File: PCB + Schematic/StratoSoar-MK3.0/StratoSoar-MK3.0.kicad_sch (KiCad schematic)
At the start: 108 parts, among them J1 Power, J10 SWD, J11 Signal, J12 Rudder, J15 Parachute, J16 Elevator, J18 USB-C, J2 Battery, J3 USB-C, J4 J Link, J8 Button, Q1 DMN1019USN-13, Q2 2N3906, Q3 DMN1019USN-13, Q4 DMN1019USN-13, Q5 2N3906, Q6 2N3906, SW1 RESET, SW2 PWR_SW, SW4 RESET, SW5 EEPROM, U11 DSK321STD, U2 ATSAMD21G18A-A, U3 MCP1700x-330xxTT, U4 ATSAMD21G18A-A, U5 BME280, U6 AT24C512C-SSHD-T, U7 ATXK-H11-E-32.768, U8 MAX-M10S, U9 MPU-9250, Y2 32.768kHz

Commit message: Commit
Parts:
- removed J10: SWD, Connector_PinHeader_2.54mm:PinHeader_1x05_P2.54mm_Vertical, symbol Connector_Generic:Conn_01x05
- added C1: 10 uF, symbol Device:C_Small
- added C2: 100 nF, symbol Device:C_Small
- added J5: Antenna, symbol Connector_Generic:Conn_01x01
- added U1: Ra-01, RF_Module:Ai-Thinker-Ra-01-LoRa, symbol RF_Module:Ai-Thinker-Ra-01
- AE1: value 1575AT43A0040001E -> 1575AT43A0040E
- C30, C32, C33: value 47uF -> 47 uF
- R11, R12, R17, R18, R20, R21: value 10K -> 10 K
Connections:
- net +3.3V: now also C1.1, C2.1, U1.3 (VDD)
- net A3: no longer J11.1 (Pin_1), J8.1 (Pin_1)
- net A4: no longer J11.2 (Pin_2)
- net A5: no longer J11.3 (Pin_3)
- net CS: now also U1.15 (~{NSS})
- net GND: now also C1.2, C2.2, U1.16 (GND), U1.2 (GND), U1.9 (GND)
- net MISO: now also U1.13 (MISO)
- net MOSI: now also U1.14 (MOSI)
- net SCK: now also U1.12 (SCK)
- net USB_IN: now also C4.1, J3.A4 (VBUS), J3.A9 (VBUS), J3.B4 (VBUS), J3.B9 (VBUS)
- net VCC: now also C30.1, C32.1, C33.1, J12.2 (Pin_2), J15.2 (Pin_2), J16.2 (Pin_2)
- removed net +5V: C30.1, C32.1, C33.1, C4.1, J12.2 (Pin_2), J15.2 (Pin_2), J16.2 (Pin_2), J3.A4 (VBUS), J3.A9 (VBUS), J3.B4 (VBUS), J3.B9 (VBUS)
- net AT_SCL: no longer names the net of J11.9 (Pin_9)
- net AT_SDA: no longer names the net of J11.8 (Pin_8)
- new net: J5.1 (Pin_1), U1.1 (ANT)
- new net LORA_RST: U1.4 (~{RESET})
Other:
- note added: "- Add ATGM336"
- note added: "LoRa module"
- note added: "RF"
- moved on the sheet: AE1, C20, C21, C22, C23, C24, C30, C33, D6, H1, H2, H3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

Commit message: IMU stuff
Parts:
- removed C32: 47 uF, Capacitor_Tantalum_SMD:CP_EIA-3528-21_Kemet-B, symbol Device:C_Polarized_Small
- removed C35: 10nF, Capacitor_SMD:C_0805_2012Metric_Pad1.18x1.45mm_HandSolder, symbol Device:C_Small
- removed C36, C42: 100nF, Capacitor_SMD:C_0805_2012Metric_Pad1.18x1.45mm_HandSolder, symbol Device:C_Small
- removed J15: Parachute, Connector_PinHeader_2.54mm:PinHeader_1x03_P2.54mm_Vertical, symbol Connector_Generic:Conn_01x03
- removed Q3: DMN1019USN-13, Package_TO_SOT_SMD:SC-59_Handsoldering, symbol Transistor_FET:DMN1019USN-13
- removed Q5: 2N3906, Package_TO_SOT_SMD:SOT-23-3, symbol Transistor_BJT:2N3906
- removed R17, R20: 10 K, Resistor_SMD:R_0805_2012Metric_Pad1.20x1.40mm_HandSolder, symbol Device:R
- removed R22: 10, Resistor_SMD:R_0805_2012Metric_Pad1.20x1.40mm_HandSolder, symbol Device:R
- removed U9: MPU-9250, Sensor_Motion:InvenSense_QFN-24_3x3mm_P0.4mm, symbol Sensor_Motion:MPU-9250
- added C10, C3, C9: 100 nF, Capacitor_SMD:C_0402_1005Metric, symbol symbols:C_Small
- added C12, C13: 1 uF, Capacitor_SMD:C_0402_1005Metric, symbol symbols:C_Small
- added Q7, Q8, Q9: BSS138, Package_TO_SOT_SMD:SOT-23, symbol symbols:BSS138
- added R13, R19, R29, R30, R31, R32: 10 K, Resistor_SMD:R_0402_1005Metric, symbol symbols:R_Small
- added U10: ICM-20948, Sensor_Motion:InvenSense_QFN-24_3x3mm_P0.4mm, symbol symbols:MPU-9250
- added U9: CJ6206B18M, Package_TO_SOT_SMD:SOT-23-5, symbol symbols:CJ6206B18M
- Q2: value 2N3906 -> MMBT3906
- R11: footprint Resistor_SMD:R_0805_2012Metric_Pad1.20x1.40mm_HandSolder -> Resistor_SMD:R_0402_1005Metric
- R12: LCSC (none) -> C25077
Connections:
- net +3.3V: now also C12.1, R19.1, R30.1, R32.1, U9.1 (VIN), U9.3 (EN)
- net GND: now also R12.2, C10.2, C12.2, C13.2, C3.2, C9.2, U10.18 (GND), U10.20 (RESV_GND), U9.2 (GND); no longer R12.1
- net at Q1.2 (G), R14.1: now also R12.1; no longer R12.2
- new net: C10.1, U10.10 (REGOUT)
- new net +1V8: C13.1, C3.1, C9.1, Q7.1 (G), Q8.1 (G), Q9.1 (G), R13.1, R29.1, R31.1, U10.13 (VDD), U10.8 (VDDIO), U9.5 (1.8V)
- new net INTH: Q9.3 (D), R32.2
- new net INTL: Q9.2 (S), R31.2, U10.12 (INT)
- new net SCLH: Q7.3 (D), R19.2
- new net SCLL: Q7.2 (S), R13.2, U10.23 (SCL/SCLK)
- new net SDAH: Q8.3 (D), R30.2
- new net SDAL: Q8.2 (S), R29.2, U10.24 (SDA/MOSI)
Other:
- note added: "IMU - ICM-20948"
- note removed: "MPU-9250 (IMU)"
- note removed: "Parachute servo and FET"
- moved on the sheet: C22, C23, SW5, U5, U6

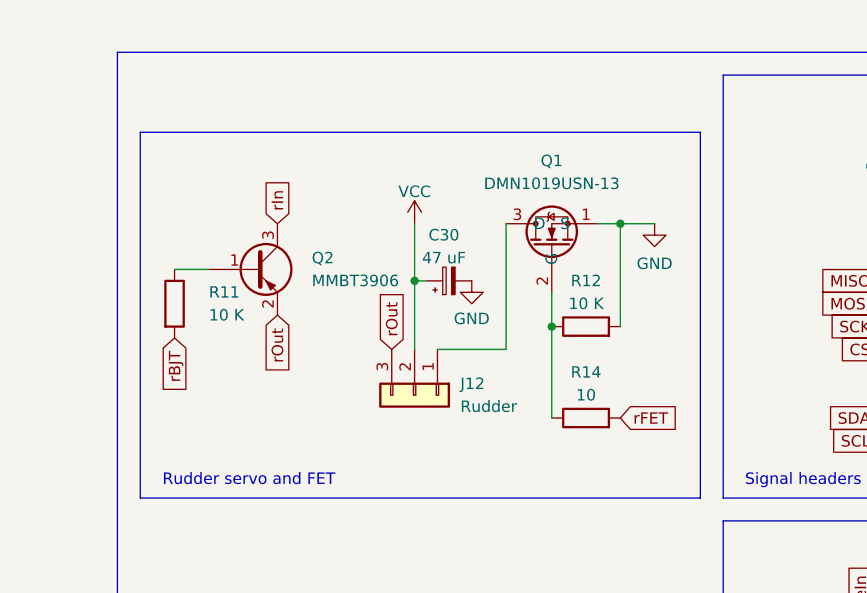
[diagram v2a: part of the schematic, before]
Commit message: Worked on servo section
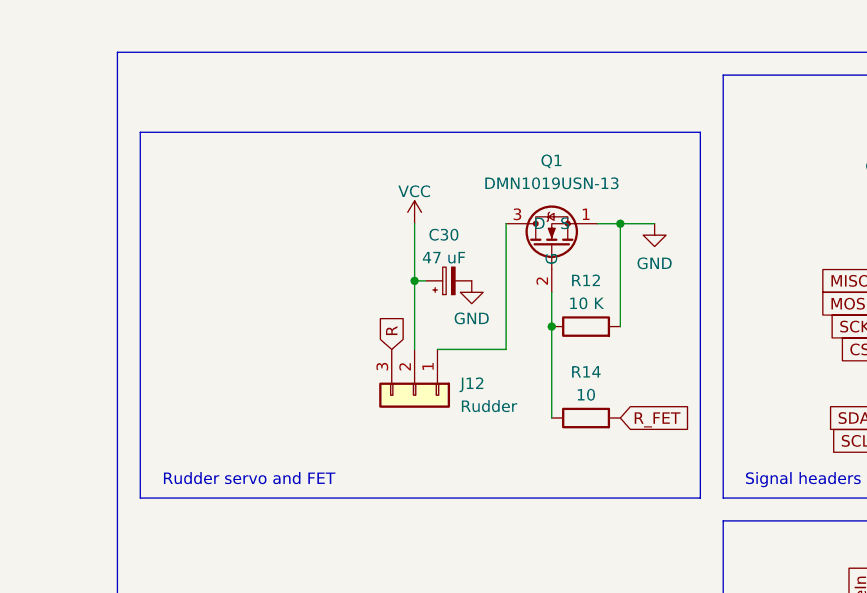
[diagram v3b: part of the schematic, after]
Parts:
- removed Q2: MMBT3906, Package_TO_SOT_SMD:SOT-23-3, symbol Transistor_BJT:2N3906
- removed R11: 10 K, Resistor_SMD:R_0402_1005Metric, symbol Device:R
- C30: footprint Capacitor_Tantalum_SMD:CP_EIA-3528-21_Kemet-B -> Capacitor_SMD:C_1206_3216Metric; LCSC (none) -> C139825
- R12, R14: footprint Resistor_SMD:R_0805_2012Metric_Pad1.20x1.40mm_HandSolder -> Resistor_SMD:R_0402_1005Metric
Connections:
- net rFET: no longer R14.2
- net rOut renamed R
- new net R_FET: R14.2
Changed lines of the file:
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@@
 	(wire
 		(pts
-			(xy -24.13 -138.43) (xy -20.32 -138.43)
-		)
-		(stroke
-			(width 0)
-			(type default)
-		)
-	)
-	(wire
-		(pts
 			(xy 17.78 -135.89) (xy 17.78 -132.08)
 		)
@@
 		)
 	)
+	(global_label "R"
+		(shape input)
+		(at 0 -129.54 90)
+		(fields_autoplaced yes)
+		(effects
+			(font
+				(size 1.27 1.27)
+			)
+			(justify left)
+		)
+		(property "Intersheetrefs" "${INTERSHEET_REFS}"
+			(at 0 -133.7952 90)
+			(effects
+				(font
+					(size 1.27 1.27)
+				)
+				(justify left)
+				(hide yes)
+			)
+		)
+	)
 	(global_label "A5"
 		(shape input)
@@
 		)
 	)
-	(global_label "rOut"
-		(shape input)
-		(at 0 -129.54 90)
-		(fields_autoplaced yes)
-		(effects
-			(font
-				(size 1.27 1.27)
-			)
-			(justify left)
-		)
-		(property "Intersheetrefs" "${INTERSHEET_REFS}"
-			(at 0 -136.5166 90)
-			(effects
-				(font
-					(size 1.27 1.27)
-				)
-				(justify left)
-				(hide yes)
-			)
-		)
-	)
 	(global_label "SCK"
 		(shape input)
@@
 		)
 	)
-	(global_label "rFET"
+	(global_label "R_FET"
 		(shape input)
 		(at 25.4 -121.92 0)
@@
 		)
 		(property "Intersheetrefs" "${INTERSHEET_REFS}"
-			(at 32.3766 -121.92 0)
+			(at 33.828 -121.92 0)
 			(effects
 				(font
@@
 		)
 	)
-	(global_label "rOut"
-		(shape input)
-		(at -12.7 -133.35 270)
-		(fields_autoplaced yes)
-		(effects
-			(font
-				(size 1.27 1.27)
-			)
-			(justify right)
-		)
-		(property "Intersheetrefs" "${INTERSHEET_REFS}"
-			(at -12.7 -126.3734 90)
-			(effects
-				(font
-					(size 1.27 1.27)
-				)
-				(justify right)
-				(hide yes)
-			)
-		)
-	)
 	(global_label "pBJT"
 		(shape input)
@@
 		)
 	)
-	(global_label "rIn"
-		(shape input)
-		(at -12.7 -143.51 90)
-		(fields_autoplaced yes)
-		(effects
-			(font
-				(size 1.27 1.27)
-			)
-			(justify left)
-		)
-		(property "Intersheetrefs" "${INTERSHEET_REFS}"
-			(at -12.7 -149.0352 90)
-			(effects
-				(font
-					(size 1.27 1.27)
-				)
-				(justify left)
-				(hide yes)
-			)
-		)
-	)
 	(global_label "USB_IN"
 		(shape input)
@@
 		)
 	)
-	(global_label "rBJT"
-		(shape input)
-		(at -24.13 -130.81 270)
-		(fields_autoplaced yes)
-		(effects
-			(font
-				(size 1.27 1.27)
-			)
-			(justify right)
-		)
-		(property "Intersheetrefs" "${INTERSHEET_REFS}"
-			(at -24.13 -123.8334 90)
-			(effects
-				(font
-					(size 1.27 1.27)
-				)
-				(justify right)
-				(hide yes)
-			)
-		)
-	)
 	(global_label "eBJT"
 		(shape input)
@@
 			)
 		)
-		(property "Footprint" "Resistor_SMD:R_0805_2012Metric_Pad1.20x1.40mm_HandSolder"
+		(property "Footprint" "Resistor_SMD:R_0402_1005Metric"
 			(at 21.59 -130.302 90)
 			(effects
@@
 			)
 		)
-		(property "Footprint" "Capacitor_Tantalum_SMD:CP_EIA-3528-21_Kemet-B"
+		(property "Footprint" "Capacitor_SMD:C_1206_3216Metric"
 			(at 6.35 -137.16 0)
 			(effects
@@
 			)
 		)
+		(property "LCSC" "C139825"
+			(at 6.35 -137.16 90)
+			(effects
+				(font
+					(size 1.27 1.27)
+				)
+				(hide yes)
+			)
+		)
 		(pin "1"
 		)
@@
 	)
 	(symbol
-		(lib_id "Device:R")
-		(at -24.13 -134.62 0)
-		(unit 1)
-		(exclude_from_sim no)
-		(in_bom yes)
-		(on_board yes)
-		(dnp no)
-		(fields_autoplaced yes)
-		(property "Reference" "R11"
-			(at -20.32 -135.8901 0)
-			(effects
-				(font
-					(size 1.27 1.27)
-				)
-				(justify left)
-			)
-		)
-		(property "Value" "10 K"
-			(at -20.32 -133.3501 0)
-			(effects
-				(font
-					(size 1.27 1.27)
-				)
-				(justify left)
-			)
-		)
-		(property "Footprint" "Resistor_SMD:R_0402_1005Metric"
-			(at -25.908 -134.62 90)
-			(effects
-				(font
-					(size 1.27 1.27)
-				)
-				(hide yes)
-			)
-		)
-		(property "Datasheet" "~"
-			(at -24.13 -134.62 0)
-			(effects
-				(font
-					(size 1.27 1.27)
-				)
-				(hide yes)
-			)
-		)
-		(property "Description" ""
-			(at -24.13 -134.62 0)
-			(effects
-				(font
-					(size 1.27 1.27)
-				)
-				(hide yes)
-			)
-		)
-		(pin "1"
-		)
-		(pin "2"
-		)
-		(instances
-			(project "StratoSoar-MK3.0"
-				(path "/a5ed86dc-e941-4edd-8d1d-eae06db8d6f6"
-					(reference "R11")
-					(unit 1)
-				)
-			)
-		)
-	)
-	(symbol
 		(lib_name "GND_15")
 		(lib_id "power:GND")
@@
 	)
 	(symbol
-		(lib_id "Transistor_BJT:2N3906")
-		(at -15.24 -138.43 0)
-		(unit 1)
-		(exclude_from_sim no)
-		(in_bom yes)
-		(on_board yes)
-		(dnp no)
-		(fields_autoplaced yes)
-		(property "Reference" "Q2"
-			(at -8.89 -139.7001 0)
-			(effects
-				(font
-					(size 1.27 1.27)
-				)
-				(justify left)
-			)
-		)
-		(property "Value" "MMBT3906"
-			(at -8.89 -137.1601 0)
-			(effects
-				(font
-					(size 1.27 1.27)
-				)
-				(justify left)
-			)
-		)
-		(property "Footprint" "Package_TO_SOT_SMD:SOT-23-3"
-			(at -10.16 -136.525 0)
-			(effects
-				(font
-					(size 1.27 1.27)
-					(italic yes)
-				)
-				(justify left)
-				(hide yes)
-			)
-		)
-		(property "Datasheet" "https://www.onsemi.com/pub/Collateral/2N3906-D.PDF"
-			(at -15.24 -138.43 0)
-			(effects
-				(font
-					(size 1.27 1.27)
-				)
-				(justify left)
-				(hide yes)
-			)
-		)
-		(property "Description" "-0.2A Ic, -40V Vce, Small Signal PNP Transistor, TO-92"
-			(at -15.24 -138.43 0)
-			(effects
-				(font
-					(size 1.27 1.27)
-				)
-				(hide yes)
-			)
-		)
-		(pin "1"
-		)
-		(pin "2"
-		)
-		(pin "3"
-		)
-		(instances
-			(project "StratoSoar-MK3.0"
-				(path "/a5ed86dc-e941-4edd-8d1d-eae06db8d6f6"
-					(reference "Q2")
-					(unit 1)
-				)
-			)
-		)
-	)
-	(symbol
 		(lib_id "Switch:SW_SPDT")
 		(at 125.73 17.78 0)
@@
 			)
 		)
-		(property "Footprint" "Resistor_SMD:R_0805_2012Metric_Pad1.20x1.40mm_HandSolder"
+		(property "Footprint" "Resistor_SMD:R_0402_1005Metric"
 			(at 21.59 -120.142 90)
 			(effects

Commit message: Organization
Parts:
- removed C14, C15, C16, C19, C34, C37, C38: 100nF, Capacitor_SMD:C_0805_2012Metric_Pad1.18x1.45mm_HandSolder, symbol Device:C_Small
- removed C17: 10uF, Capacitor_SMD:C_0805_2012Metric_Pad1.18x1.45mm_HandSolder, symbol Device:C_Small
- removed C18: 1uF, Capacitor_SMD:C_0805_2012Metric_Pad1.18x1.45mm_HandSolder, symbol Device:C_Small
- removed C21: 1 uF, Capacitor_SMD:C_0805_2012Metric_Pad1.18x1.45mm_HandSolder, symbol Device:C_Small
- removed C28, C29: 22pF, Capacitor_SMD:C_0805_2012Metric_Pad1.18x1.45mm_HandSolder, symbol Device:C_Small
- removed C31: 100pF, Capacitor_SMD:C_0805_2012Metric_Pad1.18x1.45mm_HandSolder, symbol Device:C_Small
- removed C33: 47 uF, Capacitor_Tantalum_SMD:CP_EIA-3528-21_Kemet-B, symbol Device:C_Polarized_Small
- removed D4: LED, LED_SMD:LED_0805_2012Metric_Pad1.15x1.40mm_HandSolder, symbol Device:LED
- removed D5: ERR_LED, LED_SMD:LED_0805_2012Metric_Pad1.15x1.40mm_HandSolder, symbol Device:LED
- removed FB1: BLM18AG121SN1D, Resistor_SMD:R_0603_1608Metric_Pad0.98x0.95mm_HandSolder, symbol Device:FerriteBead_Small
- removed J16: Elevator, Connector_PinHeader_2.54mm:PinHeader_1x03_P2.54mm_Vertical, symbol Connector_Generic:Conn_01x03
- removed J18: USB-C, Connector_USB:USB_C_Receptacle_GCT_USB4105-xx-A_16P_TopMnt_Horizontal, symbol Connector:USB_C_Receptacle_USB2.0
- removed JP11: LED_EN, Jumper:SolderJumper-2_P1.3mm_Open_RoundedPad1.0x1.5mm, symbol Jumper:SolderJumper_2_Open
- removed JP12: ERR_LED_EN, Jumper:SolderJumper-2_P1.3mm_Open_RoundedPad1.0x1.5mm, symbol Jumper:SolderJumper_2_Open
- removed JP8, JP9: XO_EN, Jumper:SolderJumper-2_P1.3mm_Open_RoundedPad1.0x1.5mm, symbol Jumper:SolderJumper_2_Open
- removed L1: 10uH, Inductor_SMD:L_0805_2012Metric_Pad1.15x1.40mm_HandSolder, symbol Device:L
- removed Q4: DMN1019USN-13, Package_TO_SOT_SMD:SC-59_Handsoldering, symbol Transistor_FET:DMN1019USN-13
- removed Q6: 2N3906, Package_TO_SOT_SMD:SOT-23-3, symbol Transistor_BJT:2N3906
- removed R10: 220, Resistor_SMD:R_0805_2012Metric_Pad1.20x1.40mm_HandSolder, symbol Device:R_Small
- removed R15, R16: 1.8K, Resistor_SMD:R_0805_2012Metric_Pad1.20x1.40mm_HandSolder, symbol Device:R_Small
- removed R23: 10, Resistor_SMD:R_0805_2012Metric_Pad1.20x1.40mm_HandSolder, symbol Device:R
- removed R24, R25: 5.1K, Resistor_SMD:R_0805_2012Metric_Pad1.20x1.40mm_HandSolder, symbol Device:R_Small
- removed R26, R27: 1K, Resistor_SMD:R_0805_2012Metric_Pad1.20x1.40mm_HandSolder, symbol Device:R_Small
- removed R29, R30, R31, R32: 10 K, Resistor_SMD:R_0402_1005Metric, symbol symbols:R_Small
- removed SW4: RESET, Button_Switch_SMD:SW_SPST_CK_RS282G05A3, symbol Switch:SW_Push
- removed U3: MCP1700x-330xxTT, Package_TO_SOT_SMD:SOT-89-3, symbol Regulator_Linear:MCP1700x-330xxTT
- removed U4: ATSAMD21G18A-A, Package_QFP:TQFP-48_7x7mm_P0.5mm, symbol MCU_Microchip_SAMD:ATSAMD21G18A-A
- removed U7: ATXK-H11-E-32.768, Crystal:Crystal_SMD_Abracon_ABM8AIG-4Pin_3.2x2.5mm, symbol Oscillator:ATXK-H11-E-32.768KHZ-E50-T3
- removed Y2: 32.768kHz, Crystal:Crystal_C26-LF_D2.1mm_L6.5mm_Horizontal, symbol Device:Crystal_Small
- added C27: 47 uF, Capacitor_SMD:C_1206_3216Metric, symbol Device:C_Polarized_Small
- added J6: Rudder, Connector_PinHeader_2.54mm:PinHeader_1x03_P2.54mm_Vertical, symbol Connector_Generic:Conn_01x03
- added Q2: DMN1019USN-13, Package_TO_SOT_SMD:SC-59_Handsoldering, symbol Transistor_FET:DMN1019USN-13
- added R11, R17, R20, R22: 10 K, Resistor_SMD:R_0402_1005Metric, symbol symbols:R_Small
- added U12: XC6206P332MR-G, Package_TO_SOT_SMD:SOT-23-3, symbol Regulator_Linear:XC6206PxxxMR
- C1: footprint (none) -> Capacitor_SMD:C_0603_1608Metric; LCSC (none) -> C19702
- C11: value 10uF -> 1 uF; footprint Capacitor_SMD:C_0805_2012Metric_Pad1.18x1.45mm_HandSolder -> Capacitor_SMD:C_0603_1608Metric; LCSC (none) -> C15849
- C2: footprint (none) -> Capacitor_SMD:C_0603_1608Metric; LCSC (none) -> C14663
- C20: footprint Capacitor_SMD:C_0805_2012Metric_Pad1.18x1.45mm_HandSolder -> Capacitor_SMD:C_0603_1608Metric; LCSC (none) -> C15849
- C24: footprint Capacitor_SMD:C_0805_2012Metric_Pad1.18x1.45mm_HandSolder -> Capacitor_SMD:C_0402_1005Metric; LCSC (none) -> C1523
- Q1: LCSC (none) -> C145103
- R12, R13, R19: LCSC C25077 -> C25744
- R14: LCSC (none) -> C25077
- R18: footprint Resistor_SMD:R_0805_2012Metric_Pad1.20x1.40mm_HandSolder -> Resistor_SMD:R_0402_1005Metric; LCSC (none) -> C25744
- R21: value 10 K -> 10; footprint Resistor_SMD:R_0805_2012Metric_Pad1.20x1.40mm_HandSolder -> Resistor_SMD:R_0402_1005Metric; LCSC (none) -> C25077
- R8, R9: footprint Resistor_SMD:R_0805_2012Metric_Pad1.20x1.40mm_HandSolder -> Resistor_SMD:R_0402_1005Metric; LCSC (none) -> C26083
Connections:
- net SCLH is gone; now on net SCL: Q7.3 (D), R19.2
- net SDAH is gone; now on net SDA: Q8.3 (D)
- net eBJT is gone; now on net GND: R18.2
- net +1V8: now also R11.1, R20.1
- net +3.3V: now also C11.1, R17.1, R22.1, U12.2 (VO); no longer C11.2
- net GND: now also C11.2, C27.2, Q2.1 (S), U12.1 (GND); no longer C11.1, R21.1
- net INTL: now also R20.2
- net SDA: now also R17.2
- net SDAL: now also R11.2
- net VCC: now also C27.1, J6.2 (Pin_2), U12.3 (VI)
- net at R18.1: now also R21.1, Q2.2 (G)
- net L_FET: now reaches R21.2
- net INTH renamed INT
- net INT: now also R22.2
- new net: J6.1 (Pin_1), Q2.3 (D)
- new net L: J6.3 (Pin_3)
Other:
- note added: "Add new GPS w/ decoupling"
- note added: "EDIT IMU 10 K RESISTORS"
- note added: "Left servo and FET"
- note added: "Right servo and FET"
- note removed: "- Add ATGM336"
- note removed: "- Add LoRa module"
- note removed: "32.768 kHz XO"
- note removed: "Elevator servo and FET"
- note removed: "Rudder servo and FET"
- note removed: "SAMD21G18A - Main MCU"
- company: (none) -> Hack Club/New England Sci-Tech
- title: (none) -> StratoSoar MK3
- moved on the sheet: AE1, C1, C10, C12, C13, C2, C20, C22, C23, C24, C25, C26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

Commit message: More work on the schematic
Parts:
- removed C22: 100nF, Capacitor_SMD:C_0603_1608Metric_Pad1.08x0.95mm_HandSolder, symbol Device:C_Small
- added AE3: 1575AT43A0040001E, 1575AT43A0040E:ANT_1575AT_JOT-L, symbol symbols:Antenna_Chip
- added BT1: MS621R, Battery:MS621R, symbol symbols:Battery_Cell
- added C14: 100 nF, Capacitor_SMD:C_0402_1005Metric, symbol symbols:C_Small
- added C17, C18: 100 nF, Capacitor_SMD:C_0603_1608Metric, symbol symbols:C_Small
- added D3: RED, LED_SMD:LED_0603_1608Metric, symbol symbols:LED_Small
- added L3: 33 nH, Inductor_SMD:L_0402_1005Metric, symbol symbols:L
- added R10: 1 K, Resistor_SMD:R_0402_1005Metric, symbol symbols:R_Small
- added U4: ATGM336H, RF_GPS:ATGM336H, symbol symbols:ATGM336H
- added U7: AT24CS32-STUM, Package_TO_SOT_SMD:SOT-23-5, symbol symbols:AT24CS32-STUM
- C23: value 1uF -> 1 uF; footprint Capacitor_SMD:C_0603_1608Metric_Pad1.08x0.95mm_HandSolder -> Capacitor_SMD:C_0402_1005Metric; LCSC (none) -> C52923
- C25: footprint Capacitor_SMD:C_0805_2012Metric_Pad1.18x1.45mm_HandSolder -> Capacitor_SMD:C_0402_1005Metric; LCSC (none) -> C1546
- C26: footprint Capacitor_SMD:C_0805_2012Metric_Pad1.18x1.45mm_HandSolder -> Capacitor_SMD:C_0402_1005Metric; LCSC (none) -> C1525
- C4, C5, C6, C8: LCSC C1525 -> C14663
- J4: LCSC (none) -> C2881910
- SW2, SW5: LCSC (none) -> C963206
- U5: LCSC (none) -> C92489
- U6: LCSC (none) -> C615466
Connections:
- net +3.3V: now also C14.2, C17.2, C18.1, U4.5 (EN), U4.8 (VCC), U7.4 (VCC)
- net GND: now also AE3.2 (GND), BT1.2 (-), C14.1, C17.1, C18.2, D3.1 (K), L3.2, U4.1 (GND), U4.10 (GND), U4.12 (GND), U7.2 (GND), U7.5 (WP)
- net RF: now also AE3.1 (FEED), L3.1, U4.11 (RF_IN)
- new net: D3.2 (A), R10.1
- new net PPS: R10.2, U4.4 (PPS)
- new net RESET: U4.9 (RESET)
- new net RX: U4.3 (RXD)
- new net SCL_GPS: U4.17 (SCL), U7.1 (SCL)
- new net SDA_GPS: U4.16 (SDA), U7.3 (SDA)
- new net TX: U4.2 (TXD)
- new net VBAT: BT1.1 (+), U4.6 (VBAT)

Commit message: Finished schematic, started PCB
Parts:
- removed AE1: 1575AT43A0040E, 1575AT43A0040E:ANT_1575AT_JOT-L, symbol Device:Antenna_Chip
- removed D1: PWR_LED, LED_SMD:LED_0805_2012Metric, symbol Device:LED
- removed D2: LED, LED_SMD:LED_0603_1608Metric, symbol Device:LED
- removed D6: LED, LED_SMD:LED_0805_2012Metric_Pad1.15x1.40mm_HandSolder, symbol Device:LED
- removed JP13: PPS_EN, Jumper:SolderJumper-2_P1.3mm_Open_RoundedPad1.0x1.5mm, symbol Jumper:SolderJumper_2_Open
- removed L2: 33nH, Inductor_SMD:L_0805_2012Metric_Pad1.15x1.40mm_HandSolder, symbol Device:L
- removed R28: 1K, Resistor_SMD:R_0805_2012Metric_Pad1.20x1.40mm_HandSolder, symbol Device:R_Small
- removed U8: MAX-M10S, RF_GPS:ublox_MAX, symbol RF_GPS:MAX-M10S
- added D1: PWR_RED, LED_SMD:LED_0603_1608Metric, symbol Device:LED_Small
- added D4: YELLOW, LED_SMD:LED_0603_1608Metric, symbol Device:LED_Small
- C18: footprint Capacitor_SMD:C_0603_1608Metric -> Capacitor_SMD:C_0402_1005Metric; LCSC C14663 -> C1525
- D3: value RED -> YELLOW; LCSC C2286 -> C72038
- J1: footprint (none) -> Connector_PinHeader_2.54mm:PinHeader_1x04_P2.54mm_Vertical
- J2: footprint (none) -> Connector_PinHeader_2.54mm:PinHeader_1x02_P2.54mm_Vertical
- J5: footprint (none) -> Connector_PinHeader_2.54mm:PinHeader_1x01_P2.54mm_Vertical
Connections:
- net RST is gone; now on net RESET: J4.10 (Pin_10), R7.2, SW1.2, U2.40 (~{RESET})
- net GND: now also D1.1 (K), D4.1 (K)
- net RESET: no longer U4.9 (RESET)
- net at R3.1: now also D1.2 (A)
- net at R4.1: now also D4.2 (A)
- net 13 renamed LED
- net INTL renamed INT_L
- net RF renamed GPS
- net SCLL renamed SCL_L
- net SCL_GPS renamed GPS_SCL
- net GPS_SCL: no longer U7.1 (SCL)
- net SDAL renamed SDA_L
- net SDA_GPS renamed GPS_SDA
- net GPS_SDA: now also U7.1 (SCL)
- net VBAT renamed V_BAT
- new net GPS_RST: U4.9 (RESET)
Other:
- note added: "GPS Module"
- note removed: "Add new GPS w/ decoupling"
- note removed: "GPS"
- moved on the sheet: AE3, BT1, C1, C17, C18, C2, D3, J4, J5, L3, R10, U1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
